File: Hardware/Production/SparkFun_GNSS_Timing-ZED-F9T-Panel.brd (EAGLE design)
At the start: 204.5 x 100.6 mm, 1142 parts, among them J1 Radio, J10 Qwiic Right Angle, J11 PTH, J12 Qwiic Right Angle, J15 Radio, J17 USB Female Type C Connector, J18 Qwiic Right Angle, J19 PTH, J2 Qwiic Right Angle, J20 Qwiic Right Angle, J23 Radio, J25 USB Female Type C Connector, J26 Qwiic Right Angle, J27 PTH, J28 Qwiic Right Angle, J3 PTH, J31 Radio, J33 USB Female Type C Connector, J34 Qwiic Right Angle, J35 PTH, J36 Qwiic Right Angle, J39 Radio, J4 Qwiic Right Angle, J41 USB Female Type C Connector, J42 Qwiic Right Angle, J43 PTH, J44 Qwiic Right Angle, J47 Radio, J49 USB Female Type C Connector, J5 USB Female Type C Connector, J50 Qwiic Right Angle, J51 PTH, J52 Qwiic Right Angle, J55 Radio, J57 USB Female Type C Connector, J58 Qwiic Right Angle, J59 PTH, J60 Qwiic Right Angle, J63 Radio, J9 USB Female Type C Connector, U1 U-BLOX_ZED_F9T, U10 AP2112K-3.3V, U11 U-BLOX_ZED_F9T, U12 AP2112K-3.3V, U13 U-BLOX_ZED_F9T, U14 AP2112K-3.3V, U15 U-BLOX_ZED_F9T, U16 AP2112K-3.3V, U2 AP2112K-3.3V, U3 U-BLOX_ZED_F9T, U4 U-BLOX_ZED_F9T, U5 AP2112K-3.3V, U6 AP2112K-3.3V, U7 U-BLOX_ZED_F9T, U8 AP2112K-3.3V, U9 U-BLOX_ZED_F9T

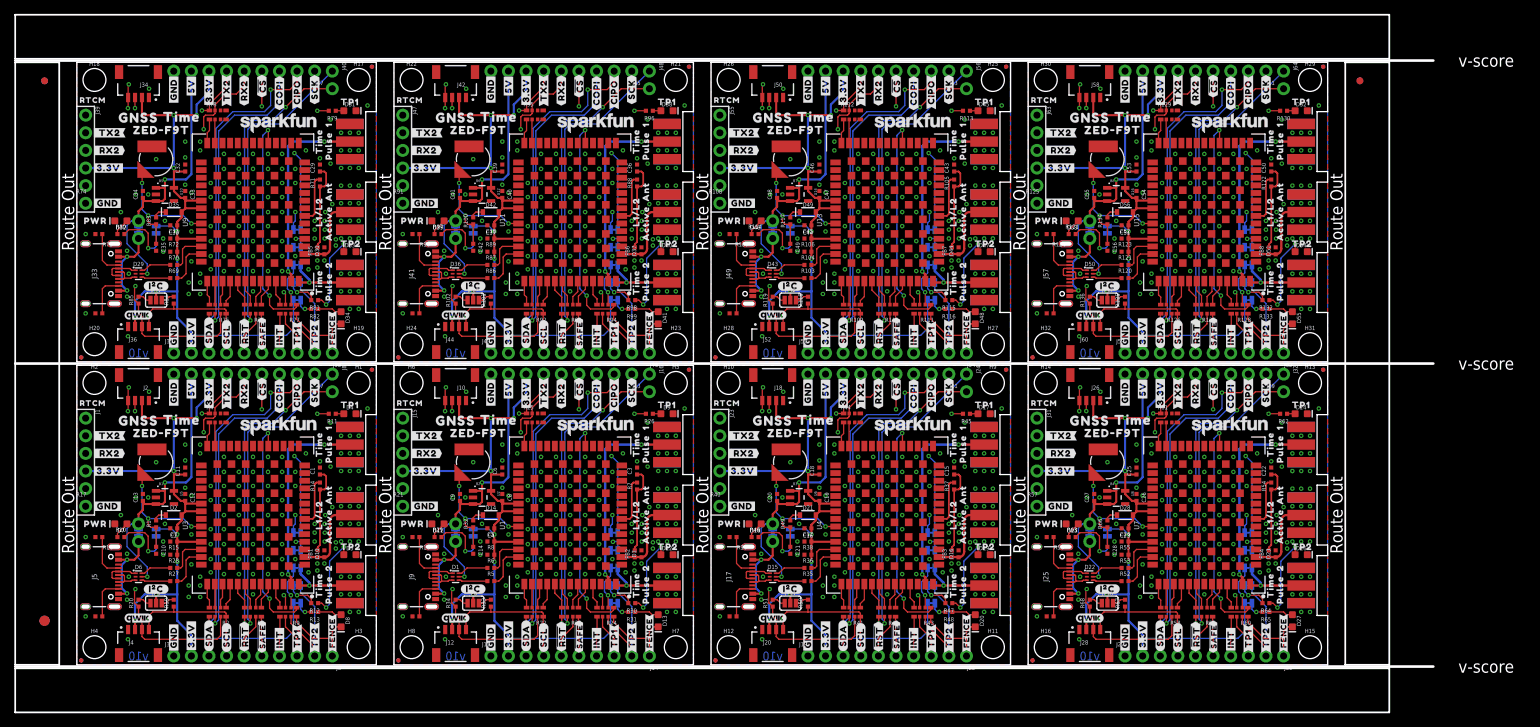
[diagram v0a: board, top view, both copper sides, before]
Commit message: Add production panel.
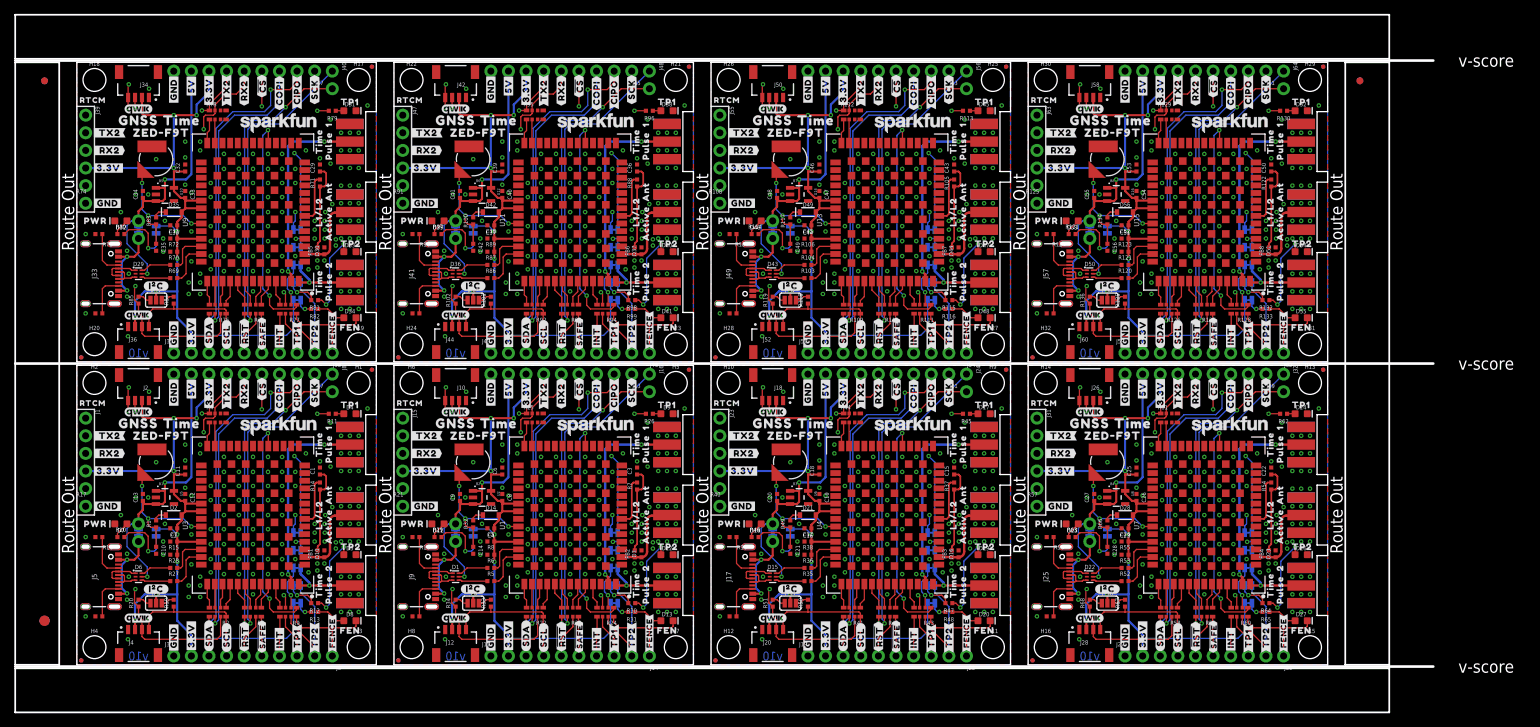
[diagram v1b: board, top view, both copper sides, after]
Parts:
- added LOGO33, LOGO35, LOGO38, LOGO40: QWIIC_LOGO_4MM, SparkFun-Aesthetics:QWIIC_4MM
- added LOGO34, LOGO39: SFE_LOGO_NAME.1_INCH, SparkFun-Aesthetics:SFE_LOGO_NAME_.1
- added LOGO36: OSHW-LOGOMINI, SparkFun-Aesthetics:OSHW-LOGO-MINI
- added LOGO37: SFE_LOGO_NAME_FLAME.1_INCH, SparkFun-Aesthetics:SFE_LOGO_NAME_FLAME_.1
- added U$609: (no value), output:##SAFE##0
- added U$610: (no value), output:RTCM0
- added U$611: (no value), output:CORRECTION1
- added U$612: (no value), output:RTCM_0
- added U$613: (no value), output:GNSS0
- added U$614: (no value), output:TIME1
- added U$615: (no value), output:ZED#F9T0
- added U$616: (no value), output:FEN0
- LOGO10, LOGO18, LOGO30: value SFE_LOGO_NAME_FLAME.1_INCH -> QWIIC_LOGO_4MM; device SparkFun-Aesthetics:SFE_LOGO_NAME_FLAME_.1 -> SparkFun-Aesthetics:QWIIC_4MM
- LOGO11, LOGO31: value QWIIC_LOGO_4MM -> OSHW-LOGOMINI; device SparkFun-Aesthetics:QWIIC_4MM -> SparkFun-Aesthetics:OSHW-LOGO-MINI
- LOGO12, LOGO32: value SFE_LOGO_NAME.1_INCH -> SFE_LOGO_NAME_FLAME.1_INCH; device SparkFun-Aesthetics:SFE_LOGO_NAME_.1 -> SparkFun-Aesthetics:SFE_LOGO_NAME_FLAME_.1
- LOGO13, LOGO25, LOGO3: value OSHW-LOGOMINI -> QWIIC_LOGO_4MM; device SparkFun-Aesthetics:OSHW-LOGO-MINI -> SparkFun-Aesthetics:QWIIC_4MM
- LOGO14: value SFE_LOGO_NAME_FLAME.1_INCH -> SFE_LOGO_NAME.1_INCH; device SparkFun-Aesthetics:SFE_LOGO_NAME_FLAME_.1 -> SparkFun-Aesthetics:SFE_LOGO_NAME_.1
- LOGO16: value SFE_LOGO_NAME.1_INCH -> OSHW-LOGOMINI; device SparkFun-Aesthetics:SFE_LOGO_NAME_.1 -> SparkFun-Aesthetics:OSHW-LOGO-MINI
- LOGO17: value OSHW-LOGOMINI -> SFE_LOGO_NAME_FLAME.1_INCH; device SparkFun-Aesthetics:OSHW-LOGO-MINI -> SparkFun-Aesthetics:SFE_LOGO_NAME_FLAME_.1
- LOGO19: value QWIIC_LOGO_4MM -> SFE_LOGO_NAME.1_INCH; device SparkFun-Aesthetics:QWIIC_4MM -> SparkFun-Aesthetics:SFE_LOGO_NAME_.1
- LOGO20, LOGO28, LOGO8: value SFE_LOGO_NAME.1_INCH -> QWIIC_LOGO_4MM; device SparkFun-Aesthetics:SFE_LOGO_NAME_.1 -> SparkFun-Aesthetics:QWIIC_4MM
- LOGO26, LOGO6: value SFE_LOGO_NAME_FLAME.1_INCH -> OSHW-LOGOMINI; device SparkFun-Aesthetics:SFE_LOGO_NAME_FLAME_.1 -> SparkFun-Aesthetics:OSHW-LOGO-MINI
- LOGO27, LOGO7: value QWIIC_LOGO_4MM -> SFE_LOGO_NAME_FLAME.1_INCH; device SparkFun-Aesthetics:QWIIC_4MM -> SparkFun-Aesthetics:SFE_LOGO_NAME_FLAME_.1
- LOGO29, LOGO9: value OSHW-LOGOMINI -> SFE_LOGO_NAME.1_INCH; device SparkFun-Aesthetics:OSHW-LOGO-MINI -> SparkFun-Aesthetics:SFE_LOGO_NAME_.1
- U$101, U$177, U$178, U$254: device output:#TX2#0 -> output:#SDA#2
- U$103, U$179, U$565: device output:#GND#2 -> output:#TX2#0
- U$104: device output:#5V#1 -> output:#GND#2
- U$105, U$259, U$336: device output:#3#3V#0 -> output:#5V#1
- U$106: device output:#SCK#5 -> output:#3#3V#0
- U$107, U$184: device output:#3#3V#0 -> output:#SCK#5
- U$109, U$128, U$165, U$185, U$186, U$204, U$205, U$262, U$281, U$337, U$414: device output:#GND#2 -> output:#3#3V#0
- U$111, U$187, U$188, U$264: device output:##RST##0 -> output:#GND#2
- U$113, U$189: device output:##SAFE##1 -> output:##RST##0
- U$114, U$191: device output:#INT#2 -> output:##SAFE##1
- U$116, U$192, U$193, U$269: device output:#TP1#3 -> output:#INT#2
- U$118, U$194, U$195, U$271: device output:#TP2#4 -> output:#TP1#3
- U$120, U$196: device output:#FENCE#0 -> output:#TP2#4
- U$121: device output:#_FENCE#0 -> output:#FENCE#0
- U$122: device output:#TP2#0 -> output:#_FENCE#0
- U$123: device output:#TP1#0 -> output:#TP2#0
- U$124: device output:#TP1_LED#0 -> output:#TP1#0
- U$125: device output:#TP2_LED#0 -> output:#TP1_LED#0
- U$126, U$203: device output:#3#3V#0 -> output:#TP2_LED#0
- U$130, U$206: device output:TP10 -> output:#GND#2
- U$131: device output:TP21 -> output:TP10
- U$132: device output:#FENCE#0 -> output:TP21
- U$133: device output:#TX_RDY#0 -> output:#FENCE#0
- U$134: device output:#D_SEL#1 -> output:#TX_RDY#0
- U$135: device output:#_TX2#0 -> output:#D_SEL#1
- U$136: device output:PWR0 -> output:#_TX2#0
- U$137: device output:#PWR#0 -> output:PWR0
- U$138: device output:#_RX2#0 -> output:#PWR#0
- U$139: device output:#RX2_#0 -> output:#_RX2#0
- U$140: device output:#TX2_#0 -> output:#RX2_#0
- U$141: device output:#MEAS#0 -> output:#TX2_#0
- U$142: device output:#I�C#0 -> output:#MEAS#0
- U$143: device output:GNSS0 -> output:#I�C#0
- U$144, U$151: device output:TIME1 -> output:GNSS0
- U$145, U$152: device output:ZED#F9T0 -> output:TIME1
- U$146: device output:##SAFE##0 -> output:ZED#F9T0
- U$147: device output:RTCM0 -> output:##SAFE##0
- U$148: device output:CORRECTION1 -> output:RTCM0
- U$149: device output:RTCM_0 -> output:CORRECTION1
- U$150: device output:GNSS0 -> output:RTCM_0
- U$153: device output:L1#L20 -> output:ZED#F9T0
- U$154, U$78: device output:ACTIVE1 -> output:FEN0
- U$155, U$386: device output:TIME0 -> output:L1#L20
- U$156, U$387: device output:PULSE1 -> output:ACTIVE1
- U$157: device output:12 -> output:TIME0
- U$158: device output:TIME0 -> output:PULSE1
- U$159: device output:PULSE1 -> output:12
- U$160, U$388: device output:20 -> output:TIME0
- U$161, U$389: device output:ANT1 -> output:PULSE1
- U$162: device output:#SCL#3 -> output:20
- U$163: device output:#3#3V#0 -> output:ANT1
- U$164, U$484: device output:#5V#1 -> output:#SCL#3
- U$166, U$243: device output:##CS##4 -> output:#5V#1
- U$167, U$90: device output:##CS##4 -> output:#GND#2
- U$168, U$169, U$245, U$92: device output:#CIPO#6 -> output:##CS##4
- U$170, U$171, U$247, U$94: device output:#COPI#5 -> output:#CIPO#6
- U$172, U$173, U$249, U$96: device output:#RX2#1 -> output:#COPI#5
- U$174, U$98: device output:#SCL#3 -> output:#RX2#1
- U$175, U$251, U$252, U$328: device output:#SDA#2 -> output:#RX2#1
- U$176, U$99: device output:#SDA#2 -> output:#SCL#3
- U$180, U$256: device output:#5V#1 -> output:#TX2#0
- U$181, U$335, U$412: device output:#3#3V#0 -> output:#GND#2
- U$182: device output:#SCK#5 -> output:#5V#1
- U$190, U$266, U$267, U$343: device output:#INT#2 -> output:##RST##0
- U$197, U$273: device output:#_FENCE#0 -> output:#TP2#4
- U$198: device output:#TP2#0 -> output:#FENCE#0
- U$199: device output:#TP1#0 -> output:#_FENCE#0
- U$200: device output:#TP1_LED#0 -> output:#TP2#0
- U$201: device output:#TP2_LED#0 -> output:#TP1#0
- U$202, U$279: device output:#3#3V#0 -> output:#TP1_LED#0
- U$207, U$283: device output:TP21 -> output:#GND#2
- U$208: device output:#FENCE#0 -> output:TP10
- U$209: device output:#TX_RDY#0 -> output:TP21
- U$210: device output:#D_SEL#1 -> output:#FENCE#0
- U$211: device output:#_TX2#0 -> output:#TX_RDY#0
- U$212: device output:PWR0 -> output:#D_SEL#1
- U$213: device output:#PWR#0 -> output:#_TX2#0
- U$214: device output:#_RX2#0 -> output:PWR0
- U$215: device output:#RX2_#0 -> output:#PWR#0
- U$216: device output:#TX2_#0 -> output:#_RX2#0
- U$217: device output:#MEAS#0 -> output:#RX2_#0
- U$218: device output:#I�C#0 -> output:#TX2_#0
- U$219: device output:GNSS0 -> output:#MEAS#0
- U$220: device output:TIME1 -> output:#I�C#0
- U$221, U$228: device output:ZED#F9T0 -> output:GNSS0
- U$222: device output:##SAFE##0 -> output:TIME1
- U$223: device output:RTCM0 -> output:ZED#F9T0
- U$224: device output:CORRECTION1 -> output:##SAFE##0
- U$225: device output:RTCM_0 -> output:RTCM0
- U$226: device output:GNSS0 -> output:CORRECTION1
- U$227: device output:TIME1 -> output:RTCM_0
- U$229: device output:L1#L20 -> output:TIME1
- U$230: device output:ACTIVE1 -> output:ZED#F9T0
- U$231, U$462: device output:TIME0 -> output:FEN0
- U$232, U$463: device output:PULSE1 -> output:L1#L20
- U$233: device output:12 -> output:ACTIVE1
- U$236: device output:20 -> output:12
- U$237, U$465: device output:ANT1 -> output:TIME0
- U$238, U$466: device output:#SCL#3 -> output:PULSE1
- U$239: device output:#3#3V#0 -> output:20
- U$240: device output:#5V#1 -> output:ANT1
- U$241, U$407: device output:#GND#2 -> output:#SCL#3
- U$242, U$319: device output:##CS##4 -> output:#3#3V#0
- U$244, U$321: device output:#CIPO#6 -> output:#GND#2
- U$246, U$322, U$323, U$399: device output:#COPI#5 -> output:##CS##4
- U$248, U$324, U$325, U$401: device output:#RX2#1 -> output:#CIPO#6
- U$250, U$326: device output:#SCL#3 -> output:#COPI#5
- U$253, U$330: device output:#TX2#0 -> output:#SCL#3
- U$255, U$331: device output:#GND#2 -> output:#SDA#2
- U$257, U$333, U$411, U$487, U$488, U$564: device output:#3#3V#0 -> output:#TX2#0
- U$258: device output:#SCK#5 -> output:#GND#2
- U$261, U$338: device output:#GND#2 -> output:#SCK#5
- U$263, U$339, U$340, U$416, U$491, U$568: device output:##RST##0 -> output:#3#3V#0
- U$265, U$341: device output:##SAFE##1 -> output:#GND#2
- U$268, U$345: device output:#TP1#3 -> output:##SAFE##1
- U$270, U$346, U$347, U$423: device output:#TP2#4 -> output:#INT#2
- U$272, U$348: device output:#FENCE#0 -> output:#TP1#3
- U$274, U$350: device output:#TP2#0 -> output:#TP2#4
- U$275: device output:#TP1#0 -> output:#FENCE#0
- U$276: device output:#TP1_LED#0 -> output:#_FENCE#0
- U$277: device output:#TP2_LED#0 -> output:#TP2#0
- U$278, U$355: device output:#3#3V#0 -> output:#TP1#0
- U$280, U$357: device output:#GND#2 -> output:#TP2_LED#0
- U$282, U$358: device output:TP10 -> output:#3#3V#0
- U$284, U$360: device output:#FENCE#0 -> output:#GND#2
- U$285: device output:#TX_RDY#0 -> output:TP10
- U$286: device output:#D_SEL#1 -> output:TP21
- U$287: device output:#_TX2#0 -> output:#FENCE#0
- U$288: device output:PWR0 -> output:#TX_RDY#0
- U$289: device output:#PWR#0 -> output:#D_SEL#1
- U$290: device output:#_RX2#0 -> output:#_TX2#0
- U$291: device output:#RX2_#0 -> output:PWR0
- U$292: device output:#TX2_#0 -> output:#PWR#0
- U$293: device output:#MEAS#0 -> output:#_RX2#0
- U$294: device output:#I�C#0 -> output:#RX2_#0
- U$295: device output:GNSS0 -> output:#TX2_#0
- U$296: device output:TIME1 -> output:#MEAS#0
- U$297: device output:ZED#F9T0 -> output:#I�C#0
- U$298: device output:##SAFE##0 -> output:GNSS0
- U$299: device output:RTCM0 -> output:TIME1
- U$300: device output:CORRECTION1 -> output:ZED#F9T0
- U$301: device output:RTCM_0 -> output:##SAFE##0
- U$302: device output:GNSS0 -> output:RTCM0
- U$303: device output:TIME1 -> output:CORRECTION1
- U$304: device output:ZED#F9T0 -> output:RTCM_0
- U$305: device output:L1#L20 -> output:GNSS0
- U$306: device output:ACTIVE1 -> output:TIME1
- U$307, U$538: device output:TIME0 -> output:ZED#F9T0
- U$308, U$539: device output:PULSE1 -> output:FEN0
- U$309: device output:12 -> output:L1#L20
- U$310, U$79: device output:TIME0 -> output:ACTIVE1
- U$311, U$80, U$83: device output:PULSE1 -> output:TIME0
- U$312, U$84: device output:20 -> output:PULSE1
- U$313: device output:ANT1 -> output:12
- U$314, U$542: device output:#SCL#3 -> output:TIME0
- U$315, U$543: device output:#3#3V#0 -> output:PULSE1
- U$316: device output:#5V#1 -> output:20
- U$317: device output:#GND#2 -> output:ANT1
- U$318, U$395: device output:##CS##4 -> output:#SCL#3
- U$320, U$397: device output:#CIPO#6 -> output:#5V#1
- U$327, U$403, U$404, U$480: device output:#SDA#2 -> output:#COPI#5
- U$329, U$405, U$406, U$482: device output:#TX2#0 -> output:#RX2#1
- U$332, U$408: device output:#5V#1 -> output:#SDA#2
- U$334, U$410: device output:#SCK#5 -> output:#TX2#0
- U$342, U$418, U$419, U$495: device output:#INT#2 -> output:#GND#2
- U$344, U$420, U$421, U$497: device output:#TP1#3 -> output:##RST##0
- U$349, U$425: device output:#_FENCE#0 -> output:#TP1#3
- U$351, U$427: device output:#TP1#0 -> output:#TP2#4
- U$352: device output:#TP1_LED#0 -> output:#FENCE#0
- U$353: device output:#TP2_LED#0 -> output:#_FENCE#0
- U$354, U$431: device output:#3#3V#0 -> output:#TP2#0
- U$356, U$433: device output:#GND#2 -> output:#TP1_LED#0
- U$359, U$435: device output:TP21 -> output:#3#3V#0
- U$361, U$437: device output:#TX_RDY#0 -> output:#GND#2
- U$362: device output:#D_SEL#1 -> output:TP10
- U$363: device output:#_TX2#0 -> output:TP21
- U$364: device output:PWR0 -> output:#FENCE#0
- U$365: device output:#PWR#0 -> output:#TX_RDY#0
- U$366: device output:#_RX2#0 -> output:#D_SEL#1
- U$367: device output:#RX2_#0 -> output:#_TX2#0
- U$368: device output:#TX2_#0 -> output:PWR0
- U$369: device output:#MEAS#0 -> output:#PWR#0
- U$370: device output:#I�C#0 -> output:#_RX2#0
- U$371: device output:GNSS0 -> output:#RX2_#0
- U$372: device output:TIME1 -> output:#TX2_#0
- U$373: device output:ZED#F9T0 -> output:#MEAS#0
- U$374: device output:##SAFE##0 -> output:#I�C#0
- U$375: device output:RTCM0 -> output:GNSS0
- U$376: device output:CORRECTION1 -> output:TIME1
- U$377: device output:RTCM_0 -> output:ZED#F9T0
- U$378: device output:GNSS0 -> output:##SAFE##0
- U$379: device output:TIME1 -> output:RTCM0
- U$380: device output:ZED#F9T0 -> output:CORRECTION1
- U$381: device output:L1#L20 -> output:RTCM_0
- U$382: device output:ACTIVE1 -> output:GNSS0
- U$383: device output:TIME0 -> output:TIME1
- U$384: device output:PULSE1 -> output:ZED#F9T0
- U$385: device output:12 -> output:FEN0
- U$390: device output:#SCL#3 -> output:12
- U$391: device output:#3#3V#0 -> output:TIME0
- U$392: device output:#5V#1 -> output:PULSE1
- U$393: device output:#GND#2 -> output:20
- U$394, U$471: device output:##CS##4 -> output:ANT1
- U$396, U$473: device output:#CIPO#6 -> output:#3#3V#0
- U$398, U$475: device output:#COPI#5 -> output:#GND#2
- U$400, U$476, U$477, U$553: device output:#RX2#1 -> output:##CS##4
- U$402, U$478: device output:#SCL#3 -> output:#CIPO#6
- U$409, U$485, U$563: device output:#3#3V#0 -> output:#SDA#2
- U$413, U$490, U$89: device output:#GND#2 -> output:#5V#1
- U$415, U$492: device output:##RST##0 -> output:#SCK#5
- U$417, U$493: device output:##SAFE##1 -> output:#3#3V#0
- U$422, U$499: device output:#TP2#4 -> output:##SAFE##1
- U$424, U$500: device output:#FENCE#0 -> output:#INT#2
- U$426, U$502: device output:#TP2#0 -> output:#TP1#3
- U$428, U$504: device output:#TP1_LED#0 -> output:#TP2#4
- U$429: device output:#TP2_LED#0 -> output:#FENCE#0
- U$430, U$507: device output:#3#3V#0 -> output:#_FENCE#0
- U$432, U$509: device output:#GND#2 -> output:#TP1#0
- U$434: device output:TP10 -> output:#TP2_LED#0
- U$436, U$512: device output:#FENCE#0 -> output:#3#3V#0
- U$438, U$514: device output:#D_SEL#1 -> output:#GND#2
- U$439: device output:#_TX2#0 -> output:TP10
- U$440: device output:PWR0 -> output:TP21
- U$441: device output:#PWR#0 -> output:#FENCE#0
- U$442: device output:#_RX2#0 -> output:#TX_RDY#0
- U$443: device output:#RX2_#0 -> output:#D_SEL#1
- U$444: device output:#TX2_#0 -> output:#_TX2#0
- U$445: device output:#MEAS#0 -> output:PWR0
- U$446: device output:#I�C#0 -> output:#PWR#0
- U$447: device output:GNSS0 -> output:#_RX2#0
- U$448: device output:TIME1 -> output:#RX2_#0
- U$449: device output:ZED#F9T0 -> output:#TX2_#0
- U$450: device output:##SAFE##0 -> output:#MEAS#0
- U$451: device output:RTCM0 -> output:#I�C#0
- U$452: device output:CORRECTION1 -> output:GNSS0
- U$453: device output:RTCM_0 -> output:TIME1
- U$454: device output:GNSS0 -> output:ZED#F9T0
- U$455: device output:TIME1 -> output:##SAFE##0
- U$456: device output:ZED#F9T0 -> output:RTCM0
- U$457: device output:L1#L20 -> output:CORRECTION1
- U$458: device output:ACTIVE1 -> output:RTCM_0
- U$459: device output:TIME0 -> output:GNSS0
- U$460: device output:PULSE1 -> output:TIME1
- U$461: device output:12 -> output:ZED#F9T0
- U$464: device output:20 -> output:ACTIVE1
- U$467: device output:#3#3V#0 -> output:12
- U$468: device output:#5V#1 -> output:TIME0
- U$469: device output:#GND#2 -> output:PULSE1
- U$470, U$547: device output:##CS##4 -> output:20
- U$472, U$549: device output:#CIPO#6 -> output:#SCL#3
- U$474, U$551: device output:#COPI#5 -> output:#5V#1
- U$479, U$555, U$556: device output:#SDA#2 -> output:#CIPO#6
- U$481, U$557, U$558: device output:#TX2#0 -> output:#COPI#5
- U$483, U$559: device output:#GND#2 -> output:#RX2#1
- U$486, U$562: device output:#SCK#5 -> output:#SDA#2
- U$494, U$570, U$571: device output:#INT#2 -> output:#3#3V#0
- U$496, U$572, U$573: device output:#TP1#3 -> output:#GND#2
- U$498, U$574, U$575: device output:#TP2#4 -> output:##RST##0
- U$501, U$577: device output:#_FENCE#0 -> output:#INT#2
- U$503, U$579: device output:#TP1#0 -> output:#TP1#3
- U$505, U$581: device output:#TP2_LED#0 -> output:#TP2#4
- U$506, U$583: device output:#3#3V#0 -> output:#FENCE#0
- U$508, U$585: device output:#GND#2 -> output:#TP2#0
- U$510: device output:TP10 -> output:#TP1_LED#0
- U$511: device output:TP21 -> output:#TP2_LED#0
- U$513, U$589: device output:#TX_RDY#0 -> output:#3#3V#0
- U$515, U$591: device output:#_TX2#0 -> output:#GND#2
- U$516: device output:PWR0 -> output:TP10
- U$517: device output:#PWR#0 -> output:TP21
- U$518: device output:#_RX2#0 -> output:#FENCE#0
- U$519: device output:#RX2_#0 -> output:#TX_RDY#0
- U$520: device output:#TX2_#0 -> output:#D_SEL#1
- U$521: device output:#MEAS#0 -> output:#_TX2#0
- U$522: device output:#I�C#0 -> output:PWR0
- U$523: device output:GNSS0 -> output:#PWR#0
- U$524: device output:TIME1 -> output:#_RX2#0
- U$525: device output:ZED#F9T0 -> output:#RX2_#0
- U$526: device output:##SAFE##0 -> output:#TX2_#0
- U$527: device output:RTCM0 -> output:#MEAS#0
- U$528: device output:CORRECTION1 -> output:#I�C#0
- U$529: device output:RTCM_0 -> output:GNSS0
- U$530: device output:GNSS0 -> output:TIME1
- U$531: device output:TIME1 -> output:ZED#F9T0
- U$532: device output:ZED#F9T0 -> output:##SAFE##0
- U$533: device output:L1#L20 -> output:RTCM0
- U$534: device output:ACTIVE1 -> output:CORRECTION1
- U$535: device output:TIME0 -> output:RTCM_0
- U$536: device output:PULSE1 -> output:GNSS0
- U$537: device output:12 -> output:TIME1
- U$540: device output:20 -> output:L1#L20
- U$541: device output:ANT1 -> output:ACTIVE1
- U$544: device output:#5V#1 -> output:12
- U$545: device output:#GND#2 -> output:TIME0
- U$546: device output:##CS##4 -> output:PULSE1
- U$548: device output:#CIPO#6 -> output:ANT1
- U$550: device output:#COPI#5 -> output:#3#3V#0
- U$552: device output:#RX2#1 -> output:#GND#2
- U$554: device output:#SCL#3 -> output:##CS##4
- U$560: device output:#5V#1 -> output:#RX2#1
- U$561, U$87: device output:#3#3V#0 -> output:#SCL#3
- U$567: device output:##RST##0 -> output:#5V#1
- U$569: device output:##SAFE##1 -> output:#SCK#5
- U$576: device output:#FENCE#0 -> output:##SAFE##1
- U$578: device output:#TP2#0 -> output:#INT#2
- U$580: device output:#TP1_LED#0 -> output:#TP1#3
- U$582: device output:#3#3V#0 -> output:#TP2#4
- U$584: device output:#GND#2 -> output:#_FENCE#0
- U$586: device output:TP10 -> output:#TP1#0
- U$587: device output:TP21 -> output:#TP1_LED#0
- U$588: device output:#FENCE#0 -> output:#TP2_LED#0
- U$590: device output:#D_SEL#1 -> output:#3#3V#0
- U$592: device output:PWR0 -> output:#GND#2
- U$593: device output:#PWR#0 -> output:TP10
- U$594: device output:#_RX2#0 -> output:TP21
- U$595: device output:#RX2_#0 -> output:#FENCE#0
- U$596: device output:#TX2_#0 -> output:#TX_RDY#0
- U$597: device output:#MEAS#0 -> output:#D_SEL#1
- U$598: device output:#I�C#0 -> output:#_TX2#0
- U$599: device output:GNSS0 -> output:PWR0
- U$600: device output:TIME1 -> output:#PWR#0
- U$601: device output:ZED#F9T0 -> output:#_RX2#0
- U$602: device output:##SAFE##0 -> output:#RX2_#0
- U$603: device output:RTCM0 -> output:#TX2_#0
- U$604: device output:CORRECTION1 -> output:#MEAS#0
- U$605: device output:RTCM_0 -> output:#I�C#0
- U$81: device output:12 -> output:PULSE1
- U$82: device output:TIME0 -> output:12
- U$85: device output:ANT1 -> output:20
- U$86: device output:#SCL#3 -> output:ANT1
- U$88: device output:#5V#1 -> output:#3#3V#0
- moved LOGO19 158.2 mm to (166.2, 34.4)
- moved LOGO17 151.3 mm to (158.8, 26.7)
- moved U$308 148.7 mm to (176.5, 4.95), turned to 0 degrees
- moved LOGO18 139.8 mm to (146.1, 6.73), flipped to the top
- moved U$305 133.4 mm to (161.8, 24.1), flipped to the bottom, turned to 0 degrees
- moved U$307 128.3 mm to (158.8, 21.6), flipped to the bottom, turned to 0 degrees
- moved U$306 125.5 mm to (155.4, 24.1), flipped to the bottom, turned to 0 degrees
- moved LOGO20 124.2 mm to (146.1, 36.4)
- moved LOGO30 104.6 mm to (54.6, 80.1), flipped to the top
- moved LOGO25 97.1 mm to (8.89, 80.1), flipped to the top
- moved U$533 80.0 mm to (93.7, 81.4), turned to 0 degrees
- moved U$535 78.0 mm to (98.3, 80.3), flipped to the bottom, turned to 0 degrees
- moved LOGO29 77.5 mm to (74.8, 78.1), flipped to the top
- moved U$458 77.0 mm to (52.6, 80.3), flipped to the bottom, turned to 0 degrees
- moved U$534 76.6 mm to (98.4, 79.0), flipped to the bottom, turned to 0 degrees
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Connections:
- net RXI/MOSI renamed RXI/COPI
- net RXI/MOSI1 renamed RXI/COPI1
- net RXI/MOSI2 renamed RXI/COPI2
- net RXI/MOSI3 renamed RXI/COPI3
- net RXI/MOSI4 renamed RXI/COPI4
- net RXI/MOSI5 renamed RXI/COPI5
- net RXI/MOSI6 renamed RXI/COPI6
- net RXI/MOSI7 renamed RXI/COPI7
- net TXO/MISO renamed TXO/CIPO
- net TXO/MISO1 renamed TXO/CIPO1
- net TXO/MISO2 renamed TXO/CIPO2
- net TXO/MISO3 renamed TXO/CIPO3
- net TXO/MISO4 renamed TXO/CIPO4
- net TXO/MISO5 renamed TXO/CIPO5
- net TXO/MISO6 renamed TXO/CIPO6
- net TXO/MISO7 renamed TXO/CIPO7
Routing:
- net FENCE_STAT3: track 12.0 -> 14.6 mm
- net FENCE_STAT2: track 12.0 -> 14.6 mm
- net FENCE_STAT1: track 12.0 -> 14.6 mm
- net FENCE_STAT7: track 12.0 -> 14.6 mm
- net FENCE_STAT6: track 12.0 -> 14.6 mm
- net FENCE_STAT: track 12.0 -> 14.6 mm
- net FENCE_STAT5: track 12.0 -> 14.6 mm
- net FENCE_STAT4: track 12.0 -> 14.6 mm
- net N$95: track 3.47 -> 4.23 mm
- net N$112: track 3.47 -> 4.23 mm
- net N$44: track 3.47 -> 4.23 mm
- net N$27: track 3.47 -> 4.23 mm
- net N$78: track 3.47 -> 4.23 mm
- net N$18: track 3.47 -> 4.23 mm
- net N$129: track 3.47 -> 4.23 mm
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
